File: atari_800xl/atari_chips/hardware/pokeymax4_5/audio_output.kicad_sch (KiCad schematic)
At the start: 17 parts, among them U2 TSV854IQ4T

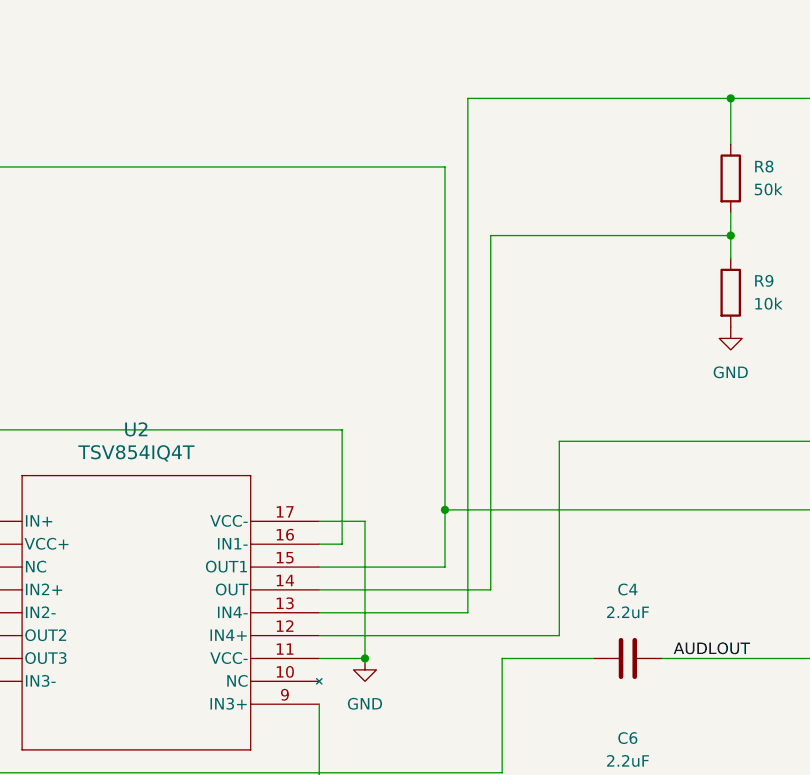
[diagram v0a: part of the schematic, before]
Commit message: After testing 4b first run, there are a few issues. Updated to 4b2 with: Corrected L/R output. ADC bias improvement. ADC preamp out/in- corrected. Moved silkscreen name!
git-svn-id: svn+ssh://192.168.0.3/home/svnfpga/repo/trunk@1476 d6161ac3-aae1-4d52-9b05-ea9ac36b53d3
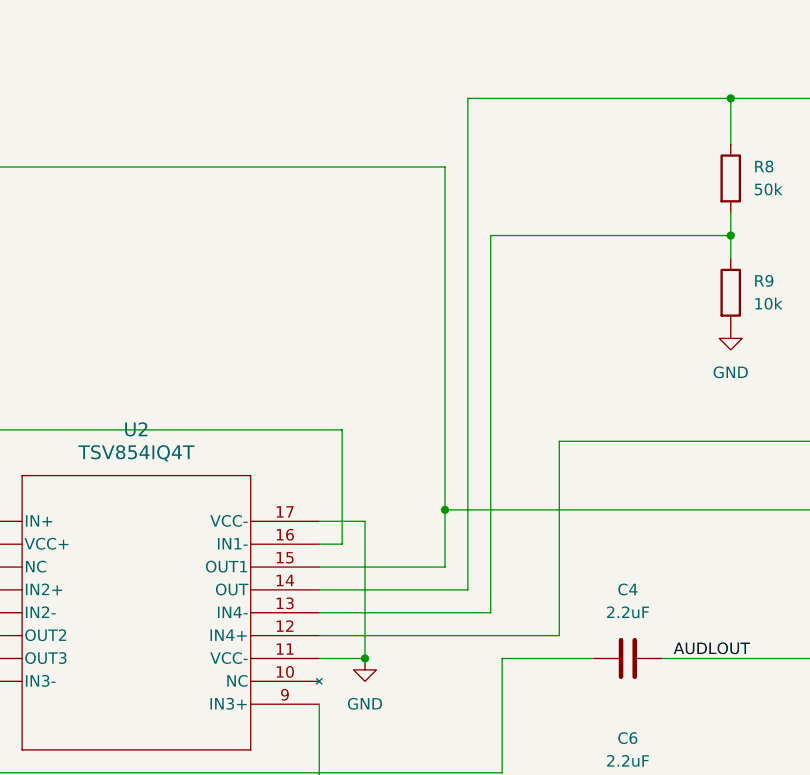
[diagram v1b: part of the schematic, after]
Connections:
- net AUD_IN_AMP: now also U2.14 (OUT); no longer U2.13 (IN4-)
- net at R8.2, R9.1: now also U2.13 (IN4-); no longer U2.14 (OUT)
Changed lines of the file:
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@@
 	(wire
 		(pts
-			(xy 173.99 57.15) (xy 173.99 114.3)
-		)
-		(stroke
-			(width 0)
-			(type default)
-		)
-	)
-	(wire
-		(pts
-			(xy 176.53 72.39) (xy 176.53 111.76)
+			(xy 173.99 57.15) (xy 173.99 111.76)
+		)
+		(stroke
+			(width 0)
+			(type default)
+		)
+	)
+	(wire
+		(pts
+			(xy 176.53 72.39) (xy 176.53 114.3)
 		)
 		(stroke
@@
 	(wire
 		(pts
+			(xy 157.48 114.3) (xy 176.53 114.3)
+		)
+		(stroke
+			(width 0)
+			(type default)
+		)
+	)
+	(wire
+		(pts
 			(xy 171.45 102.87) (xy 261.62 102.87)
 		)
@@
 	(wire
 		(pts
-			(xy 157.48 114.3) (xy 173.99 114.3)
-		)
-		(stroke
-			(width 0)
-			(type default)
-		)
-	)
-	(wire
-		(pts
 			(xy 203.2 69.85) (xy 203.2 72.39)
 		)
@@
 	(wire
 		(pts
+			(xy 157.48 111.76) (xy 173.99 111.76)
+		)
+		(stroke
+			(width 0)
+			(type default)
+		)
+	)
+	(wire
+		(pts
 			(xy 106.68 69.85) (xy 106.68 119.38)
 		)
@@
 		)
 		(stroke
-			(width 0)
-			(type default)
-		)
-	)
-	(wire
-		(pts
-			(xy 157.48 111.76) (xy 176.53 111.76)
-		)
-		(stroke

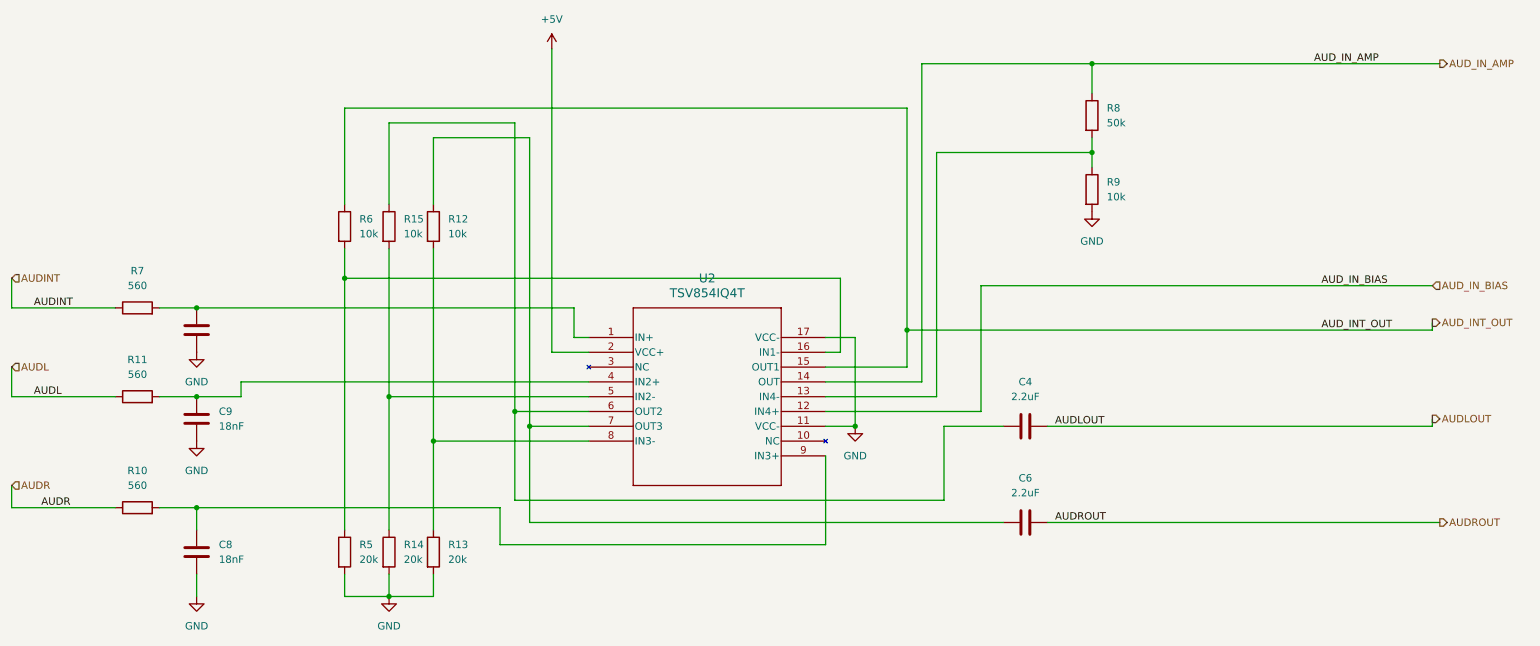
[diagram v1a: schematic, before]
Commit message: Pokeymax v4_53 as produced
git-svn-id: svn+ssh://192.168.0.3/home/svnfpga/repo/trunk@1512 d6161ac3-aae1-4d52-9b05-ea9ac36b53d3
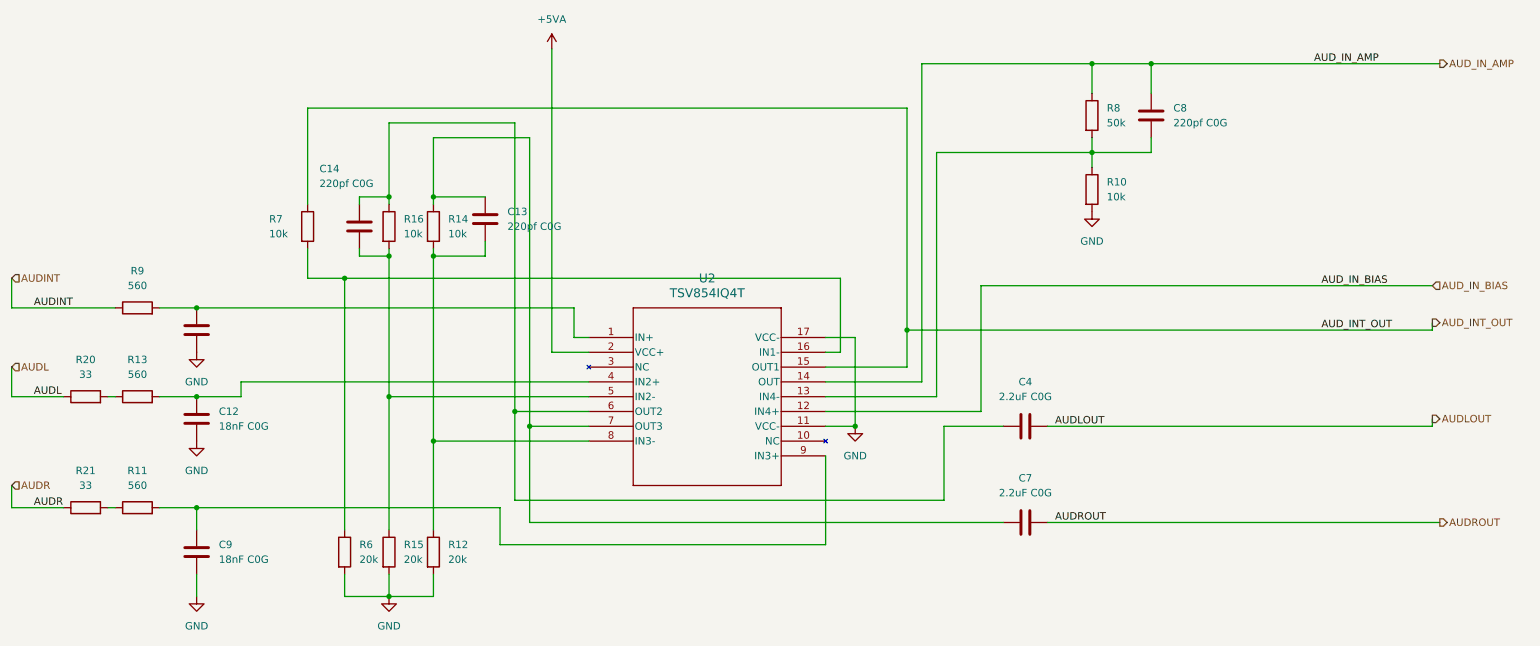
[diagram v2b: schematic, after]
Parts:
- added C13, C14, C8: 220pf C0G, Capacitor_SMD:C_0402_1005Metric, symbol Device:C
- added R20, R21: 33, Resistor_SMD:R_0402_1005Metric, symbol Device:R
- C12: renamed from C9; value 18nF -> 18nF C0G
- C4: value 2.2uF -> 2.2uF C0G
- C6: renamed from C5; value 18nF -> 18nF C0G
- C7: renamed from C6; value 2.2uF -> 2.2uF C0G
- C9: renamed from C8; value 18nF -> 18nF C0G
- renumbered R9 to R10, R10 to R11, R13 to R12, R11 to R13, R12 to R14, R14 to R15, R15 to R16, R5 to R6, R6 to R7, R7 to R9
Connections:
- net AUDL: now also R20.1; no longer R13.1
- net AUDR: now also R21.1; no longer R11.1
- net AUD_IN_AMP: now also C8.1
- net at C4.1, R16.1, U2.6 (OUT2): now also C14.1
- net at C7.1, R14.1, U2.7 (OUT3): now also C13.1
- net at R12.1, R14.2, U2.8 (IN3-): now also C13.2
- net at R10.1, R8.2, U2.13 (IN4-): now also C8.2
- net at R15.1, R16.2, U2.5 (IN2-): now also C14.2
- net +5V renamed +5VA
- new net: R11.1, R21.2
- new net: R13.1, R20.2
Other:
- moved on the sheet: R7
